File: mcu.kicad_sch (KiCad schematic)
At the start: 16 parts, among them J1 Conn_ARM_JTAG_SWD_20, U6 STM32F469VETx

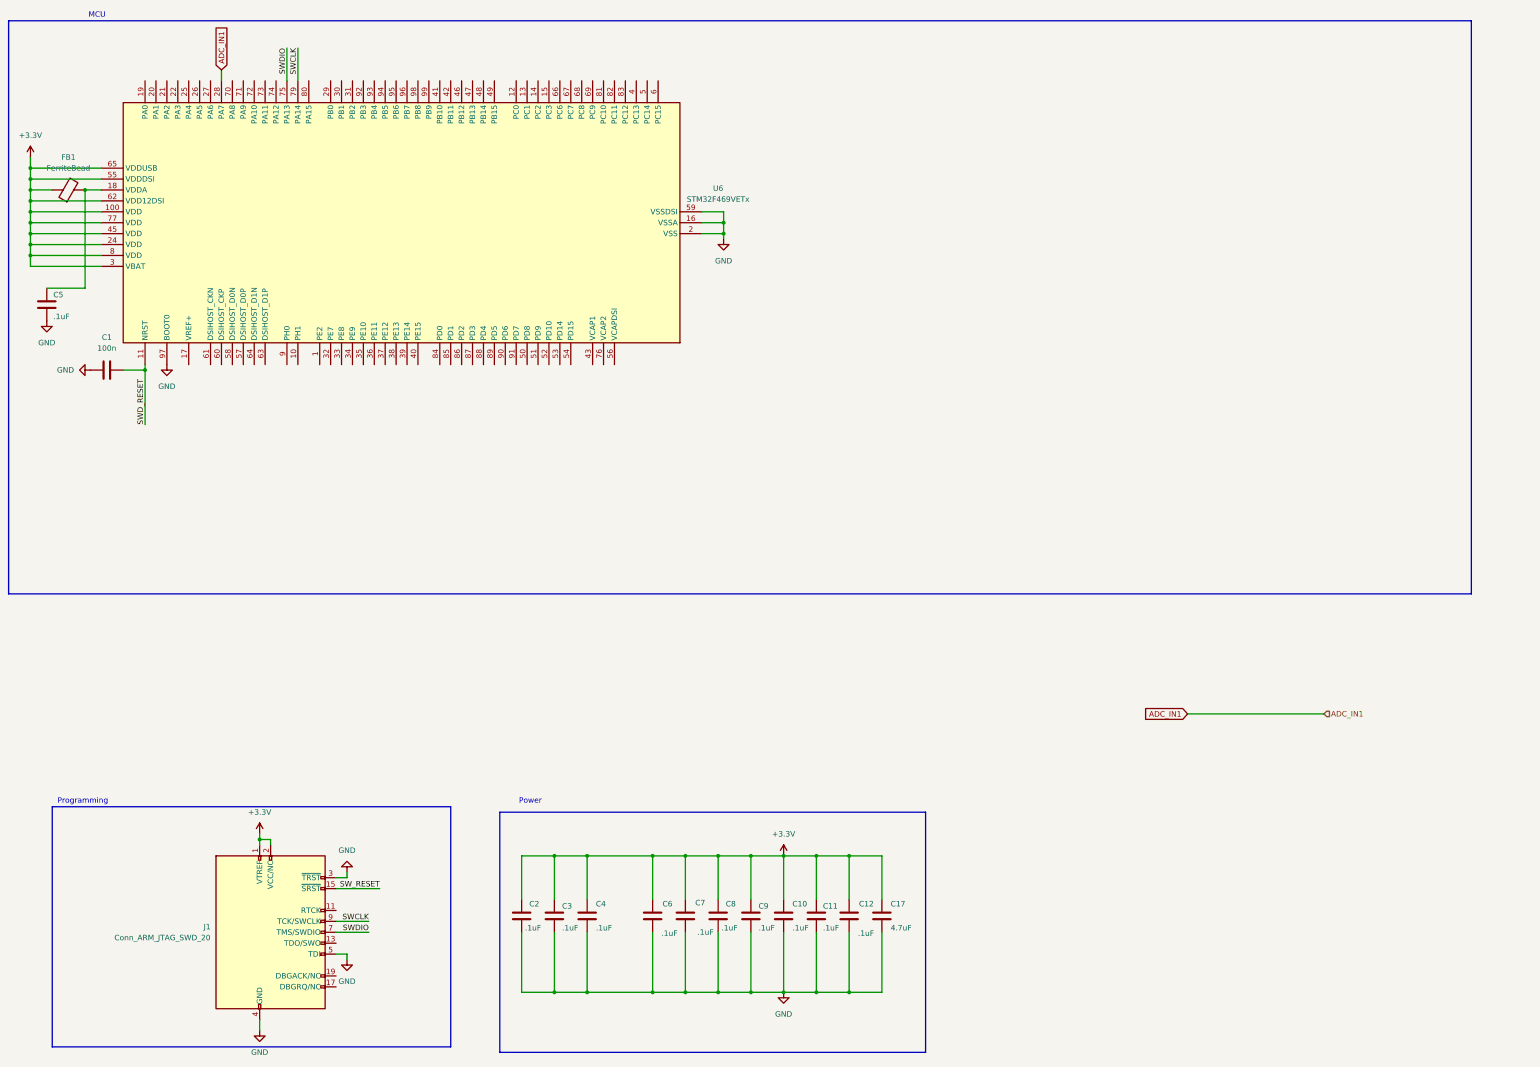
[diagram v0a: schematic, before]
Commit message: cleaned up MCU and added some debugging circuitry
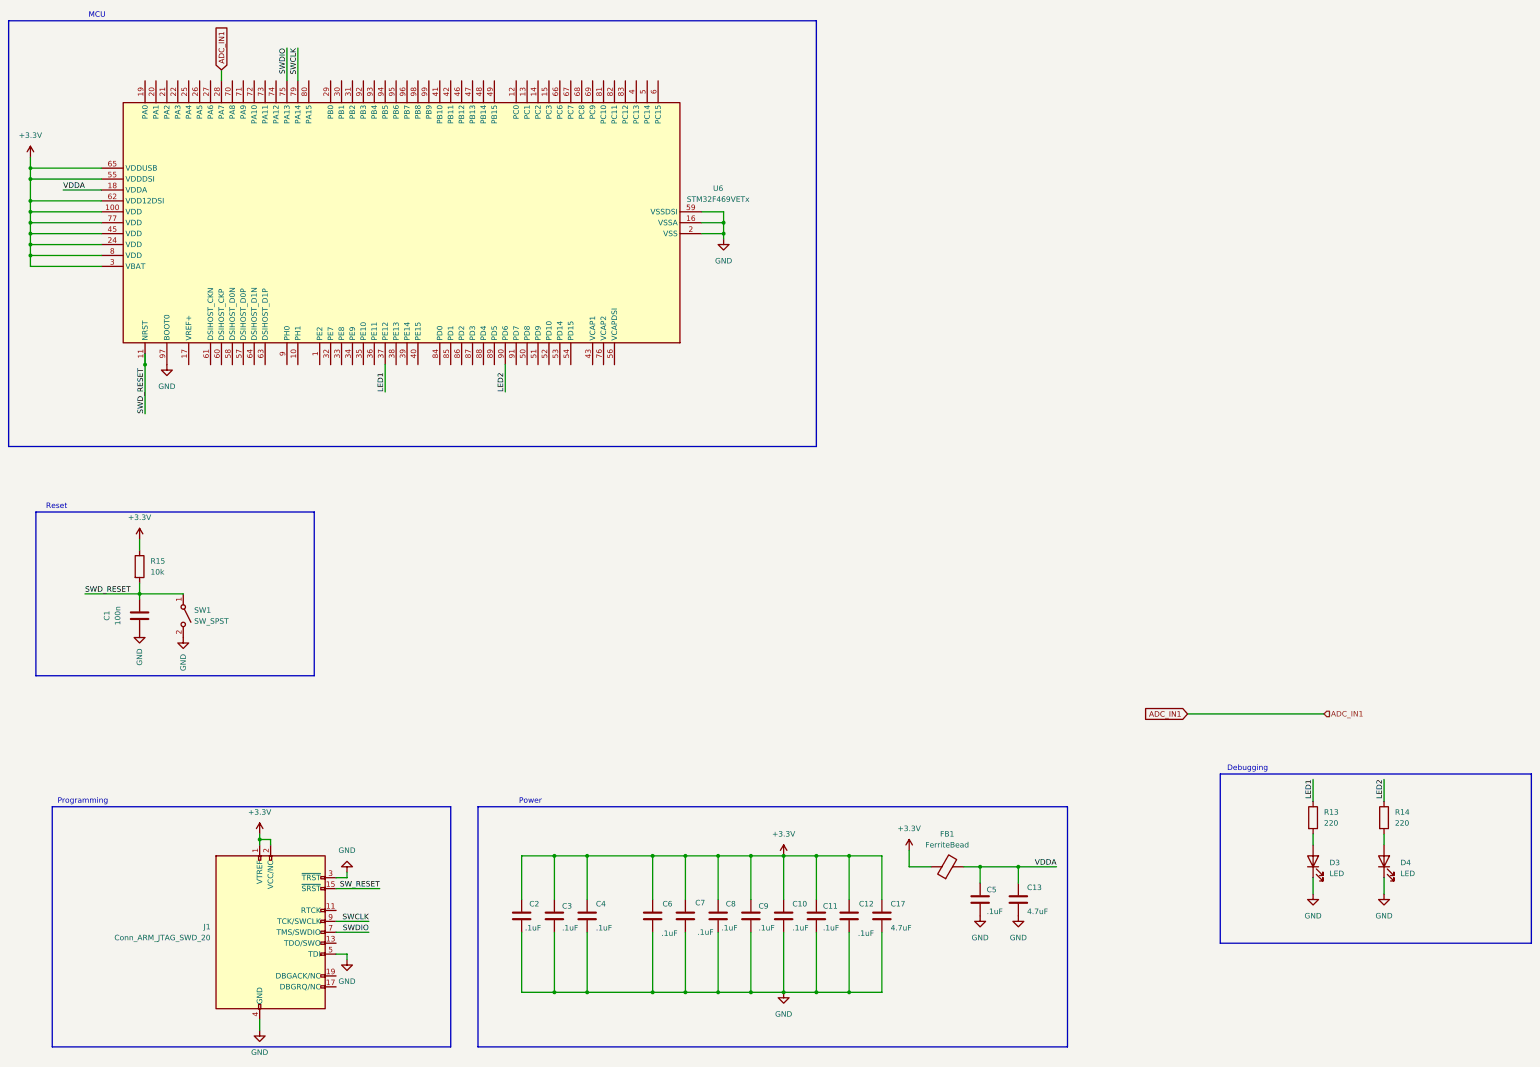
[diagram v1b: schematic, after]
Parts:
- added C13: 4.7uF, Capacitor_SMD:C_0805_2012Metric, symbol Device:C
- added D3, D4: LED, LED_SMD:LED_0805_2012Metric, symbol Device:LED
- added R13, R14: 220, Resistor_SMD:R_0805_2012Metric, symbol Device:R
- added R15: 10k, symbol Device:R
- added SW1: SW_SPST, symbol Switch:SW_SPST
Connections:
- net +3.3V: now also R15.1
- net GND: now also C13.2, D3.1 (K), D4.1 (K), SW1.2 (B)
- net SWD_RESET: now also R15.2, SW1.1 (A)
- net VDDA: now reaches C5.1, FB1.2, U6.18 (VDDA)
- net VDDA: now also C13.1
- net LED1: now reaches U6.37 (PE12)
- net LED1: now also R13.1
- net LED2: now reaches U6.90 (PD6)
- net LED2: now also R14.1
- new net: D4.2 (A), R14.2
- new net: D3.2 (A), R13.2
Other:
- note added: "Debugging"
- note added: "Reset"
- moved on the sheet: C1, C5, FB1

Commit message: schematic finish
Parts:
- R15: footprint (none) -> Resistor_SMD:R_0805_2012Metric
- SW1: footprint (none) -> Button_Switch_SMD:SW_Push_1P1T_NO_Vertical_Wuerth_434133025816
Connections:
- net INT: now reaches U6.42 (PB11)
- net CS: now reaches U6.46 (PB12)
- net SCK: now reaches U6.47 (PB13)
- net MISO: now reaches U6.48 (PB14)
- net MOSI: now reaches U6.49 (PB15)
- net WAIT: now reaches U6.50 (PD8)
- net RST: now reaches U6.52 (PD10)

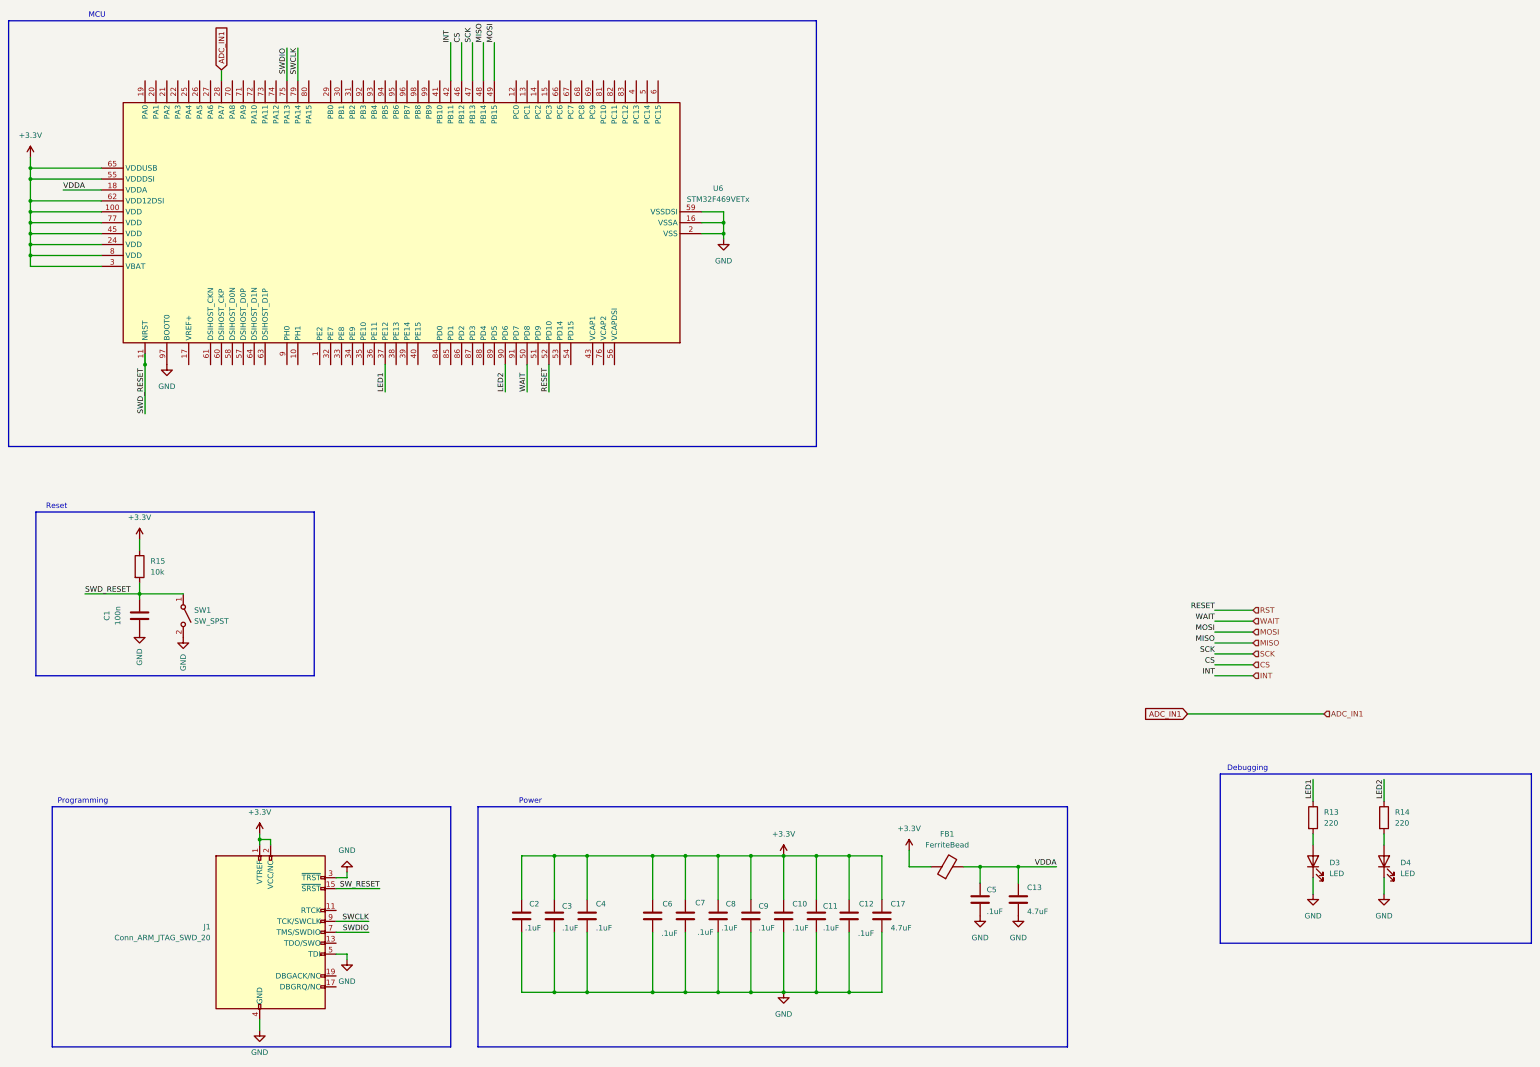
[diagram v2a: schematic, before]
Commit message: added memory and fixed clock
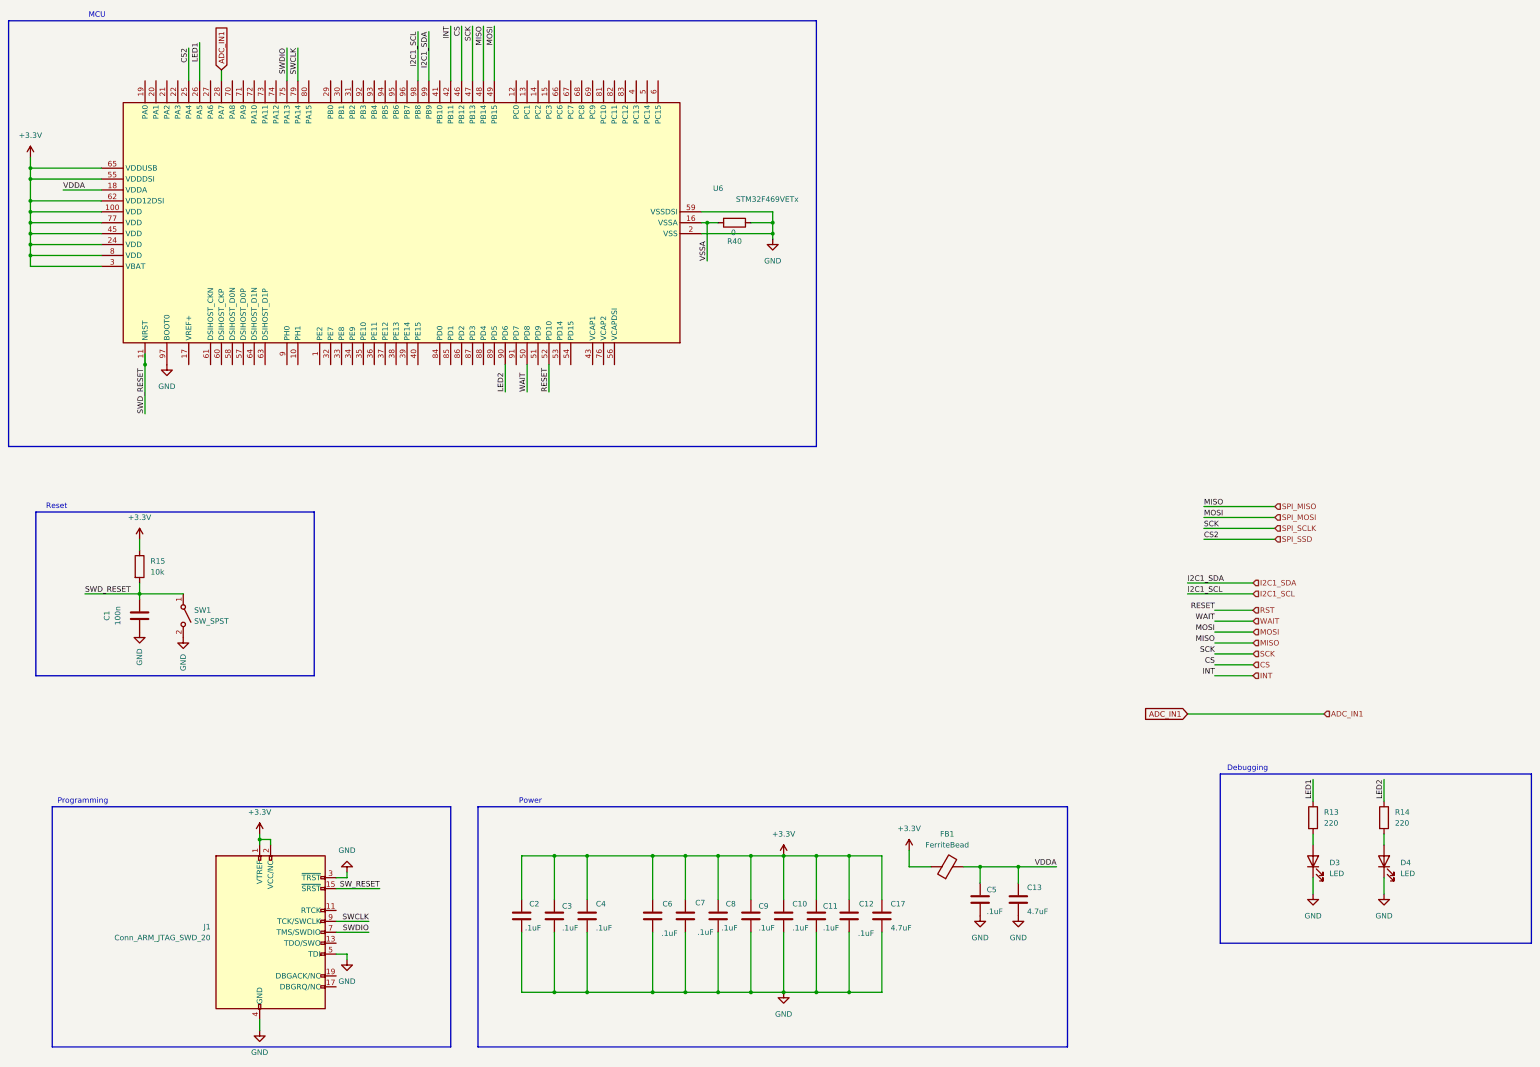
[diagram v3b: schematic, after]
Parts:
- added R40: 0, Resistor_SMD:R_0805_2012Metric, symbol Device:R
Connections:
- net GND: now also R40.1; no longer U6.16 (VSSA)
- net LED1: now also U6.26 (PA5); no longer U6.37 (PE12)
- net SPI_SSD: now reaches U6.25 (PA4)
- net I2C1_SCL: now reaches U6.98 (PB8)
- net I2C1_SDA: now reaches U6.99 (PB9)
- new net VSSA: R40.2, U6.16 (VSSA)

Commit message: Updated Schematic
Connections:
- net LED1: now also U6.27 (PA6); no longer U6.26 (PA5)
- new net DAC_OUT1: U6.26 (PA5)
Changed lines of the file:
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@@
+	(wire
+		(pts
+			(xy 58.42 34.29) (xy 64.77 34.29)
+		)
+		(stroke
+			(width 0)
+			(type default)
+		)
+	)
 	(wire
 		(pts
@@
 	(wire
 		(pts
+			(xy 67.31 36.83) (xy 67.31 44.45)
+		)
+		(stroke
+			(width 0)
+			(type default)
+		)
+	)
+	(wire
+		(pts
 			(xy 298.45 143.51) (xy 314.96 143.51)
 		)
@@
 	(wire
 		(pts
-			(xy 64.77 35.56) (xy 64.77 44.45)
+			(xy 294.64 198.12) (xy 326.39 198.12)
 		)
 		(stroke
@@
 		(pts
 			(xy 52.07 107.95) (xy 52.07 110.49)
+		)
+		(stroke
+			(width 0)
+			(type default)
+		)
+	)
+	(wire
+		(pts
+			(xy 64.77 34.29) (xy 64.77 44.45)
 		)
 		(stroke
@@
 		)
 	)
+	(label "LED1"
+		(at 67.31 36.83 270)
+		(effects
+			(font
+				(size 1.27 1.27)
+			)
+			(justify right bottom)
+		)
+	)
 	(label "CS"
 		(at 125.73 31.75 270)
@@
 	(label "SWCLK"
 		(at 87.63 36.83 270)
-		(effects
-			(font
-				(size 1.27 1.27)
-			)
-			(justify right bottom)
-		)
-	)
-	(label "LED1"
-		(at 64.77 35.56 270)
 		(effects
 			(font
@@
 		)
 	)
+	(global_label "DAC_OUT1"
+		(shape input)
+		(at 58.42 34.29 180)
+		(fields_autoplaced yes)
+		(effects
+			(font
+				(size 1.27 1.27)
+			)
+			(justify right)
+		)
+		(property "Intersheetrefs" "${INTERSHEET_REFS}"
+			(at 46.0005 34.29 0)
+			(effects
+				(font
+					(size 1.27 1.27)
+				)
+				(justify right)
+				(hide yes)
+			)
+		)
+	)
+	(global_label "DAC_OUT1"
+		(shape input)
+		(at 294.64 198.12 180)
+		(fields_autoplaced yes)
+		(effects
+			(font
+				(size 1.27 1.27)
+			)
+			(justify right)
+		)
+		(property "Intersheetrefs" "${INTERSHEET_REFS}"
+			(at 282.2205 198.12 0)
+			(effects
+				(font
+					(size 1.27 1.27)
+				)
+				(justify right)
+				(hide yes)
+			)
+		)
+	)
 	(global_label "ADC_IN1"
 		(shape input)
@@
 		(effects
 			(font
+				(size 1.27 1.27)
+			)
+			(justify left)
+		)
+	)
+	(hierarchical_label "AUDIO_OUT"
+		(shape input)
+		(at 326.39 198.12 0)
+		(effects
+			(font

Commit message: Updated Schematic
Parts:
- added U10: WE-TVS-824015043, Package_TO_SOT_SMD:SOT-23-6, symbol Power_Protection:WE-TVS-824015043
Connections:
- net +3.3V: now also U10.5 (VBUS)
- net GND: now also U10.2 (GND); no longer C13.2, C5.2
- net SWCLK: now also U10.3 (I/O2)
- net SWDIO: now also U10.6 (I/O4)
- net SW_RESET: now also U10.1 (I/O1)
- net VSSA renamed GNDA
- net GNDA: now also C13.2, C5.2

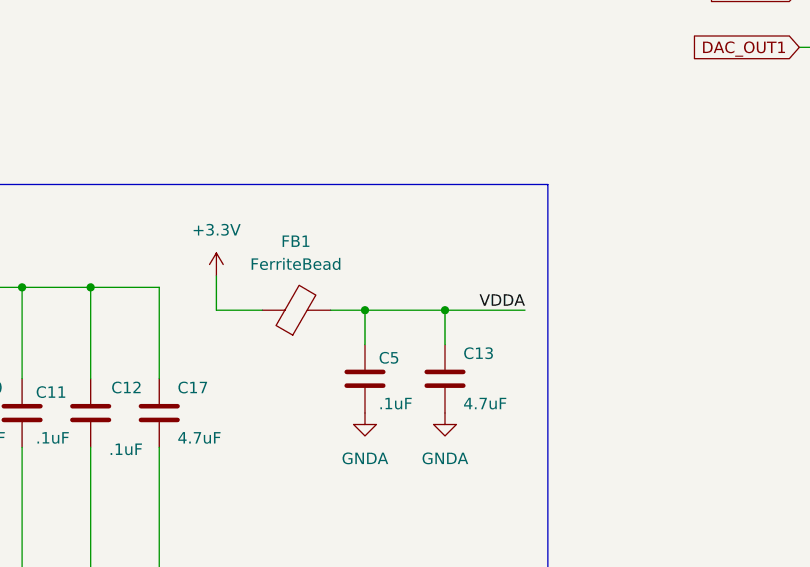
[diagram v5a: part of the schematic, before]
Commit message: rearranged HE and SD, added analog power plane
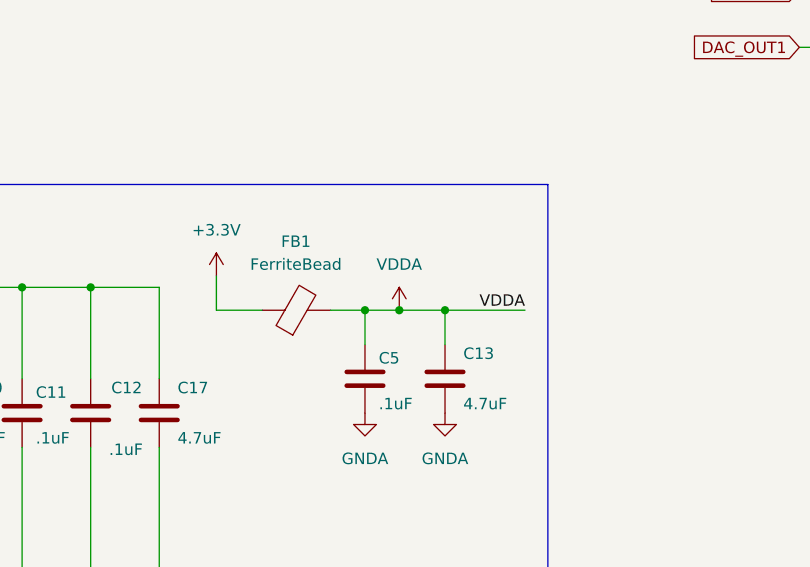
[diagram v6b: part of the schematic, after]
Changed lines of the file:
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@@
 	)
 	(junction
+		(at 250.19 227.33)
+		(diameter 0)
+		(color 0 0 0 0)
+	)
+	(junction
 		(at 200.66 224.79)
 		(diameter 0)
@@
 	(wire
 		(pts
-			(xy 246.38 227.33) (xy 255.27 227.33)
+			(xy 246.38 227.33) (xy 250.19 227.33)
 		)
 		(stroke
@@
 	(wire
 		(pts
+			(xy 250.19 227.33) (xy 255.27 227.33)
+		)
+		(stroke
+			(width 0)
+			(type default)
+		)
+	)
+	(wire
+		(pts
 			(xy 69.85 41.91) (xy 69.85 44.45)
 		)
@@
 					(unit 1)
 				)
+			)
+		)
+	)
+	(symbol
+		(lib_id "power:VDDA")
+		(at 250.19 227.33 0)
+		(unit 1)
+		(exclude_from_sim no)
+		(in_bom yes)
+		(on_board yes)
+		(dnp no)
+		(fields_autoplaced yes)
+		(property "Reference" "#PWR078"
+			(at 250.19 231.14 0)
+			(effects
+				(font
+					(size 1.27 1.27)
+				)
+				(hide yes)
+			)
+		)
+		(property "Value" "VDDA"
+			(at 250.19 222.25 0)
+			(effects
+				(font
+					(size 1.27 1.27)
+				)
+			)
+		)
+		(property "Footprint" ""
+			(at 250.19 227.33 0)
+			(effects
+				(font
+					(size 1.27 1.27)
+				)
+				(hide yes)
+			)
+		)
+		(property "Datasheet" ""
+			(at 250.19 227.33 0)
+			(effects
+				(font
+					(size 1.27 1.27)
+				)
+				(hide yes)
+			)
+		)
+		(property "Description" "Power symbol creates a global label with name \"VDDA\""
+			(at 250.19 227.33 0)
+			(effects
+				(font
+					(size 1.27 1.27)
+				)
+				(hide yes)
+			)
+		)
+		(pin "1"
+		)
+		(instances
+			(project ""
+				(path "/35c074f0-8545-4dc1-a57d-3ef0bc7d9188/332aa9c6-46d1-4f07-ac6a-0c48b9b46fa2"
+					(reference "#PWR078")
+					(unit 1)
+				)
